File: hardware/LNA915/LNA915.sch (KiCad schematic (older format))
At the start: 32 parts, among them P1 HACKRF, P2 ANTENNA, U1 SWITCH, U2 SAW, U3 LNA

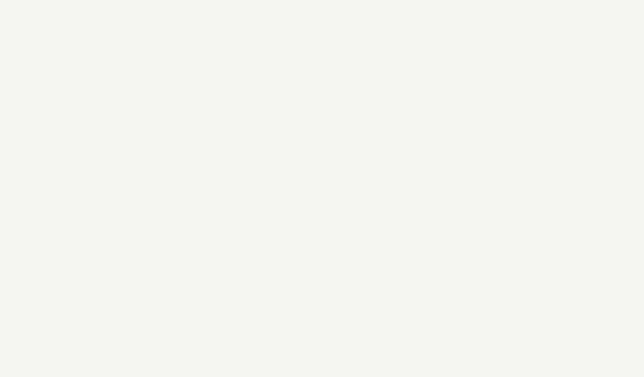
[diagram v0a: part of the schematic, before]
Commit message: LNA915 grounded mounting holes
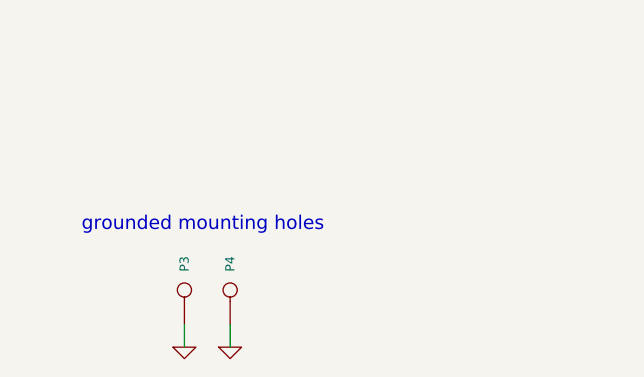
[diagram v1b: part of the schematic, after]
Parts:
- added P3, P4: CONN_1, symbol CONN_1
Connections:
- net GND: now also P3.1, P4.1
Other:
- note added: "grounded mounting holes"
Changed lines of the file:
@@
 Sheet 1 1
 Title ""
-Date "8 feb 2014"
+Date "9 feb 2014"
 Rev ""
 Comp ""
@@
 	1    0    0    1
 $EndComp
+$Comp
+L CONN_1 P3
+U 1 1 52F7A9D0
+P 1700 6650
+F 0 "P3" H 1780 6650 40  0000 L CNN
+F 1 "CONN_1" H 1700 6705 30  0001 C CNN
+F 2 "" H 1700 6650 60  0000 C CNN
+F 3 "" H 1700 6650 60  0000 C CNN
+	1    1700 6650
+	0    -1   -1   0
+$EndComp
+$Comp
+L CONN_1 P4
+U 1 1 52F7A9E7
+P 1900 6650
+F 0 "P4" H 1980 6650 40  0000 L CNN
+F 1 "CONN_1" H 1900 6705 30  0001 C CNN
+F 2 "" H 1900 6650 60  0000 C CNN
+F 3 "" H 1900 6650 60  0000 C CNN
+	1    1900 6650
+	0    -1   -1   0
+$EndComp
+$Comp
+L GND #PWR028
+U 1 1 52F7A9EF
+P 1700 6900
+F 0 "#PWR028" H 1700 6900 30  0001 C CNN
+F 1 "GND" H 1700 6830 30  0001 C CNN
+F 2 "" H 1700 6900 60  0000 C CNN
+F 3 "" H 1700 6900 60  0000 C CNN
+	1    1700 6900
+	1    0    0    -1
+$EndComp
+$Comp
+L GND #PWR029
+U 1 1 52F7A9FC
+P 1900 6900
+F 0 "#PWR029" H 1900 6900 30  0001 C CNN
+F 1 "GND" H 1900 6830 30  0001 C CNN
+F 2 "" H 1900 6900 60  0000 C CNN
+F 3 "" H 1900 6900 60  0000 C CNN
+	1    1900 6900
+	1    0    0    -1
+$EndComp
+Wire Wire Line
+	1900 6800 1900 6900
+Wire Wire Line
+	1700 6800 1700 6900
+Text Notes 1250 6400 0    60   ~ 0
+grounded mounting holes
 $EndSCHEMATC

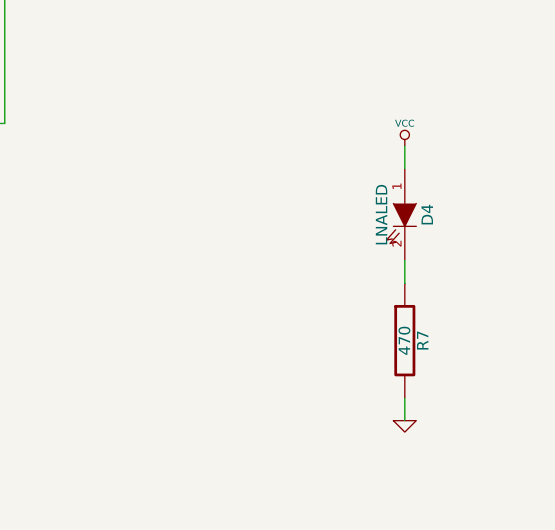
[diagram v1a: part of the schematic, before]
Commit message: LNA915 reversed LED orientation to reduce assembly confusion
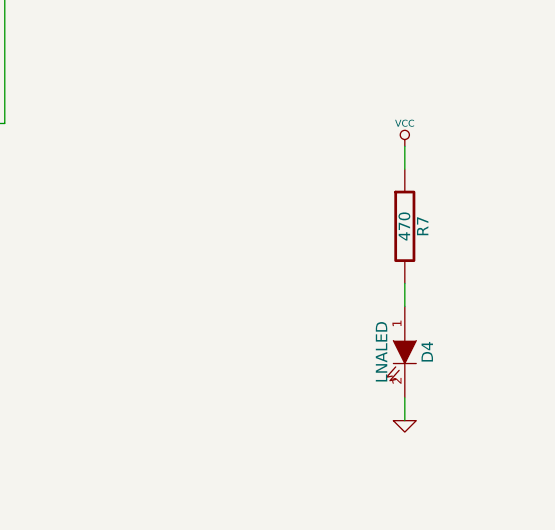
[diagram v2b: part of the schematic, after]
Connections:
- net GND: now also D4.2 (K); no longer R7.2
- net VCC: now also R7.1; no longer D4.1 (A)
- new net: D4.1 (A), R7.2
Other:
- moved on the sheet: D4, R7
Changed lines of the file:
@@
 L LED D4
 U 1 1 52F51772
-P 10400 5650
-F 0 "D4" H 10400 5750 50  0000 C CNN
-F 1 "LNALED" H 10400 5550 50  0000 C CNN
-F 2 "" H 10400 5650 60  0000 C CNN
-F 3 "" H 10400 5650 60  0000 C CNN
-F 4 "Everlight" H 10400 5650 60  0001 C CNN "Manufacturer"
-F 5 "QTLP601C4TR" H 10400 5650 60  0001 C CNN "Part Number"
-F 6 "LED GREEN STD BRIGHT 0603 SMD" H 10400 5650 60  0001 C CNN "Description"
-	1    10400 5650
+P 10400 6250
+F 0 "D4" H 10400 6350 50  0000 C CNN
+F 1 "LNALED" H 10400 6150 50  0000 C CNN
+F 2 "" H 10400 6250 60  0000 C CNN
+F 3 "" H 10400 6250 60  0000 C CNN
+F 4 "Everlight" H 10400 6250 60  0001 C CNN "Manufacturer"
+F 5 "QTLP601C4TR" H 10400 6250 60  0001 C CNN "Part Number"
+F 6 "LED GREEN STD BRIGHT 0603 SMD" H 10400 6250 60  0001 C CNN "Description"
+	1    10400 6250
 	0    1    1    0
 $EndComp
@@
 L R R7
 U 1 1 52F68CBB
-P 10400 6200
-F 0 "R7" V 10480 6200 50  0000 C CNN
-F 1 "470" V 10400 6200 50  0000 C CNN
-F 2 "" H 10400 6200 60  0000 C CNN
-F 3 "" H 10400 6200 60  0000 C CNN
-F 4 "Stackpole" H 10400 6200 60  0001 C CNN "Manufacturer"
-F 5 "RMCF0402JT470R" H 10400 6200 60  0001 C CNN "Part Number"
-F 6 "RES TF 1/16W 470 OHM 5% 0402" H 10400 6200 60  0001 C CNN "Description"
-	1    10400 6200
+P 10400 5700
+F 0 "R7" V 10480 5700 50  0000 C CNN
+F 1 "470" V 10400 5700 50  0000 C CNN
+F 2 "" H 10400 5700 60  0000 C CNN
+F 3 "" H 10400 5700 60  0000 C CNN
+F 4 "Stackpole" H 10400 5700 60  0001 C CNN "Manufacturer"
+F 5 "RMCF0402JT470R" H 10400 5700 60  0001 C CNN "Part Number"
+F 6 "RES TF 1/16W 470 OHM 5% 0402" H 10400 5700 60  0001 C CNN "Description"
+	1    10400 5700
 	1    0    0    -1
 $EndComp
@@
 Wire Wire Line
 	10400 5350 10400 5450
-Wire Wire Line
-	10400 5850 10400 5950
 Wire Wire Line
 	10400 6450 10400 6550
@@
 Text Notes 1250 6400 0    60   ~ 0
 grounded mounting holes
+Wire Wire Line
+	10400 5950 10400 6050
 $EndSCHEMATC
